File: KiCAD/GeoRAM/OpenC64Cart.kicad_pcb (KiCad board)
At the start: 2 copper layers, 94.7 x 58.4 mm, 10 parts, among them U1 74HC04, U2 74LS08, U3 74LS00, U4 74LS573, U5 74LS573, U6 74HC245, U7 C64-Exp-Port

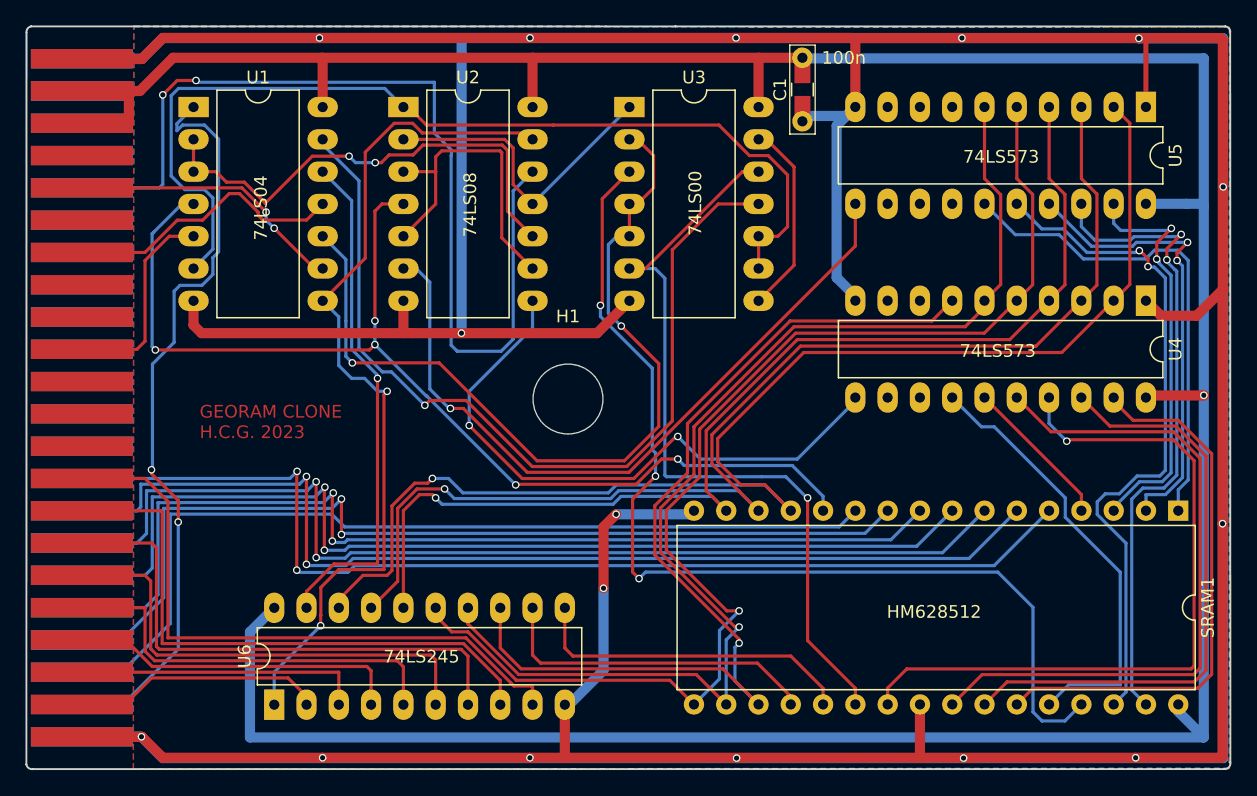
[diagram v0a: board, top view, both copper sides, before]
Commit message: Fixed some problems on the PCB that prevent the correct parsing on PCBWay
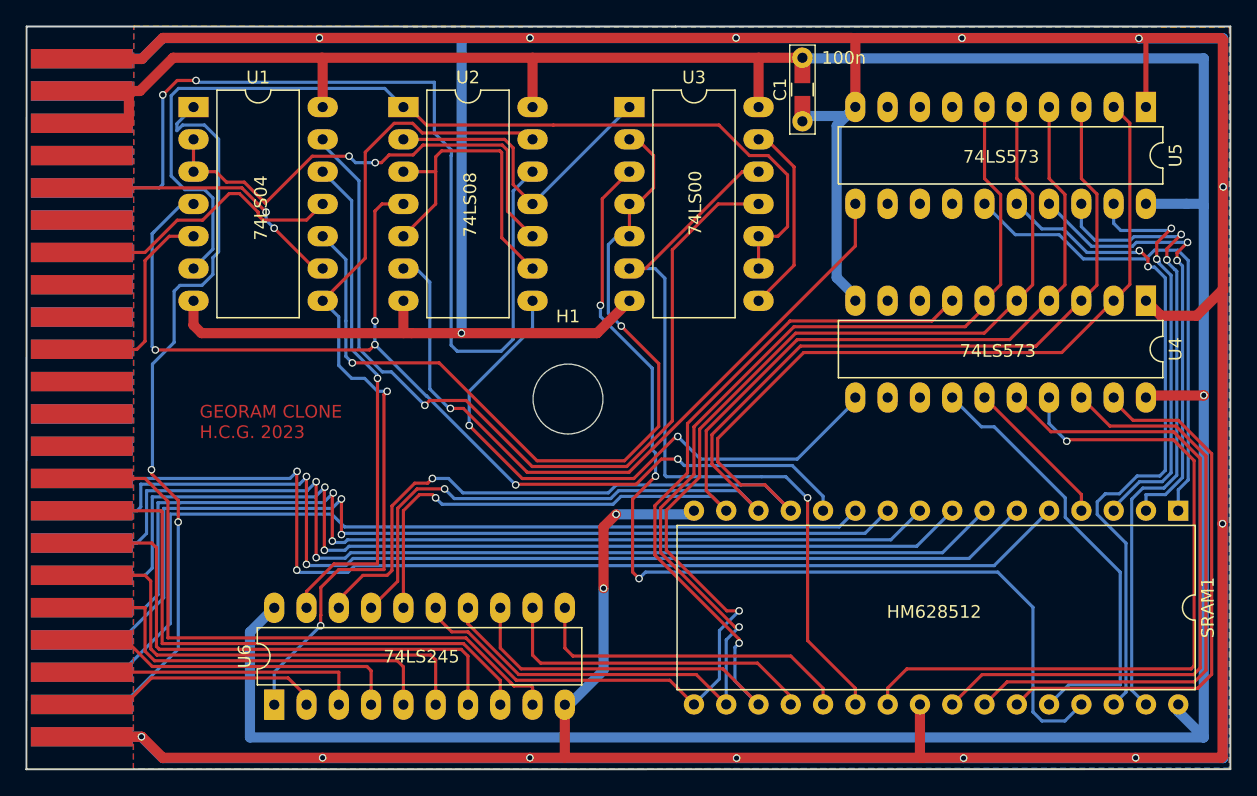
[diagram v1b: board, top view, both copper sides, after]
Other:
- outline, holes or cut-outs redrawn
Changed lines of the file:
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@@
     )
   )
-  (gr_line (start 103.24 117.621) (end 103.25 60.07) (layer "Edge.Cuts") (width 0.15))
-  (gr_arc (start 197.5612 59.563) (mid 197.810547 59.685336) (end 197.937364 59.932435) (layer "Edge.Cuts") (width 0.15))
-  (gr_line (start 103.62 59.56) (end 154.293 59.56) (layer "Edge.Cuts") (width 0.15))
-  (gr_line (start 197.5358 117.983) (end 103.74247 117.985873) (layer "Edge.Cuts") (width 0.15))
-  (gr_line (start 197.937364 59.932435) (end 197.951888 117.472755) (layer "Edge.Cuts") (width 0.15))
-  (gr_arc (start 103.25 60.07) (mid 103.331787 59.74012) (end 103.62 59.56) (layer "Edge.Cuts") (width 0.15))
-  (gr_arc (start 103.74247 117.985873) (mid 103.417727 117.904665) (end 103.24 117.621) (layer "Edge.Cuts") (width 0.15))
-  (gr_arc (start 197.951888 117.472755) (mid 197.855027 117.818544) (end 197.5358 117.983) (layer "Edge.Cuts") (width 0.15))
-  (gr_line (start 154.293 59.56) (end 197.5612 59.563) (layer "Edge.Cuts") (width 0.15))
+  (gr_line (start 103.24 118) (end 103.26 59.57) (layer "Edge.Cuts") (width 0.15))
+  (gr_line (start 103.26 59.57) (end 154.293 59.57) (layer "Edge.Cuts") (width 0.15))
+  (gr_line (start 197.95 117.99) (end 103.24 118) (layer "Edge.Cuts") (width 0.15))
+  (gr_line (start 197.95 59.57) (end 197.95 117.99) (layer "Edge.Cuts") (width 0.15))
+  (gr_line (start 154.293 59.57) (end 197.95 59.57) (layer "Edge.Cuts") (width 0.15))
   (gr_text "GEORAM CLONE\nH.C.G. 2023\n" (at 116.8654 90.678) (layer "F.Cu")
     (effects (font (size 1 1) (thickness 0.2)) (justify left))

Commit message: Version 2.0, fixed several issues with the original design
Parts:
- added C1: 100n, Capacitor_THT:C_Disc_D3.0mm_W1.6mm_P2.50mm, F.Cu at (184.9, 80.4)
- added C2: 100n, Capacitor_THT:C_Disc_D3.0mm_W1.6mm_P2.50mm, F.Cu at (124.4, 63.1)
- added C3: 100n, Capacitor_THT:C_Disc_D3.0mm_W1.6mm_P2.50mm, F.Cu at (114.6, 115.4)
- added C4: 100n, Capacitor_THT:C_Disc_D3.0mm_W1.6mm_P2.50mm, F.Cu at (184.8, 94.2)
- added C5: 100n, Capacitor_THT:C_Disc_D3.0mm_W1.6mm_P2.50mm, F.Cu at (148.4, 63.5)
- added C8: 100n, Capacitor_THT:C_Disc_D3.0mm_W1.6mm_P2.50mm, F.Cu at (185.3, 115.5)
- C7: renamed from C1; footprint OpenC64Cart:C_0805+THT -> Capacitor_THT:C_Disc_D3.0mm_W1.6mm_P2.50mm
- U1: value 74HC04 -> 7404; footprint Package_DIP:DIP-14_W10.16mm_LongPads -> Package_DIP:DIP-14_W7.62mm
- U2: value 74LS08 -> 7408; footprint Package_DIP:DIP-14_W10.16mm_LongPads -> Package_DIP:DIP-14_W7.62mm
- U3: value 74LS00 -> 7400; footprint Package_DIP:DIP-14_W10.16mm_LongPads -> Package_DIP:DIP-14_W7.62mm
- U4, U5, U6: footprint Package_DIP:DIP-20_W7.62mm_LongPads -> Package_DIP:DIP-20_W7.62mm
- moved C7 28.1 mm to (136.2, 63.4), turned to 180 degrees
- moved U3 12.4 mm to (138.3, 66.4)
- moved U5 10.1 mm to (182.2, 70.3)
- moved U4 9.61 mm to (182.2, 84.1)
- moved SRAM1 9.39 mm to (184.5, 98.0)
- moved U2 6.86 mm to (126.1, 66.4)
- moved U6 5.01 mm to (117.7, 112.8)
- moved U1 2.23 mm to (114.2, 66.4)
- moved U7 0.31 mm to (103.5, 59.3)
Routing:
- net GND: track 608.2 -> 466.9 mm, vias 16 -> 4
- net /A17: track 53.4 -> 118.5 mm, vias 2 -> 1
- net /A15: track 51.0 -> 107.4 mm, vias 2 -> 1
- net /A8: track 43.4 -> 91.1 mm, vias 0 -> 2
- net /A13: track 34.9 -> 79.4 mm
- net /A9: track 47.1 -> 90.1 mm, vias 0 -> 2
- net PHI: track 75.9 -> 37.3 mm, vias 2 -> 1
- net ~{CS} SRAM: track 61.6 -> 100.2 mm, vias 1 -> 2
- net +5V: track 259.5 -> 287.1 mm, vias 1 -> 2
- net /A11: track 53.6 -> 80.8 mm
- net Net-(U1-Pad13): track 69.7 -> 42.6 mm, vias 1 -> 0
- net /D1: track 96.1 -> 121.2 mm, vias 1 -> 3
- net /A10: track 57.0 -> 79.8 mm, vias 1 -> 0
- net Net-(U1-Pad6): track 76.0 -> 53.8 mm
- net /D2: track 89.0 -> 110.7 mm, vias 1 -> 2
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- added copper zone on B.Cu, net (none)
- added copper zone on F.Cu, net (none)
- removed copper zone on B.Cu, net GND
- removed copper zone on F.Cu, net GND
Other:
- board size 94.7 x 58.4 mm -> 84 x 58.2 mm
- board text added: "74HC00"
- board text added: "74HC04"
- board text added: "74HC08"
- board text added: "74HC245"
- board text added: "74HC573"
- board text added: "@DFFE"
- board text added: "@DFFF"
- board text added: "Home Computer Group 2023 GeoRAM clone 512K"
- board text added: "THIS SIDE UP"
- board text removed: "100n"
- board text removed: "74LS00"
- board text removed: "74LS04"
- board text removed: "74LS08"
- board text removed: "74LS245"
- board text removed: "74LS573"
- board text removed: "GEORAM CLONE H.C.G. 2023"
